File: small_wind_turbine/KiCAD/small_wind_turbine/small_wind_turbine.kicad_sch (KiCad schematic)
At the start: 50 parts, among them J1 Conn_01x03_Male, J2 Conn_01x03_Male, K1 FINDER-36.11, SW1 SW_Push_SPDT, U2 UC2844A, U3 IRS10752LPBF, U4 Opamp_Quad, U7 MCP3021, U8 MCP4725xxx-xCH, U9 AZ1117-5.0

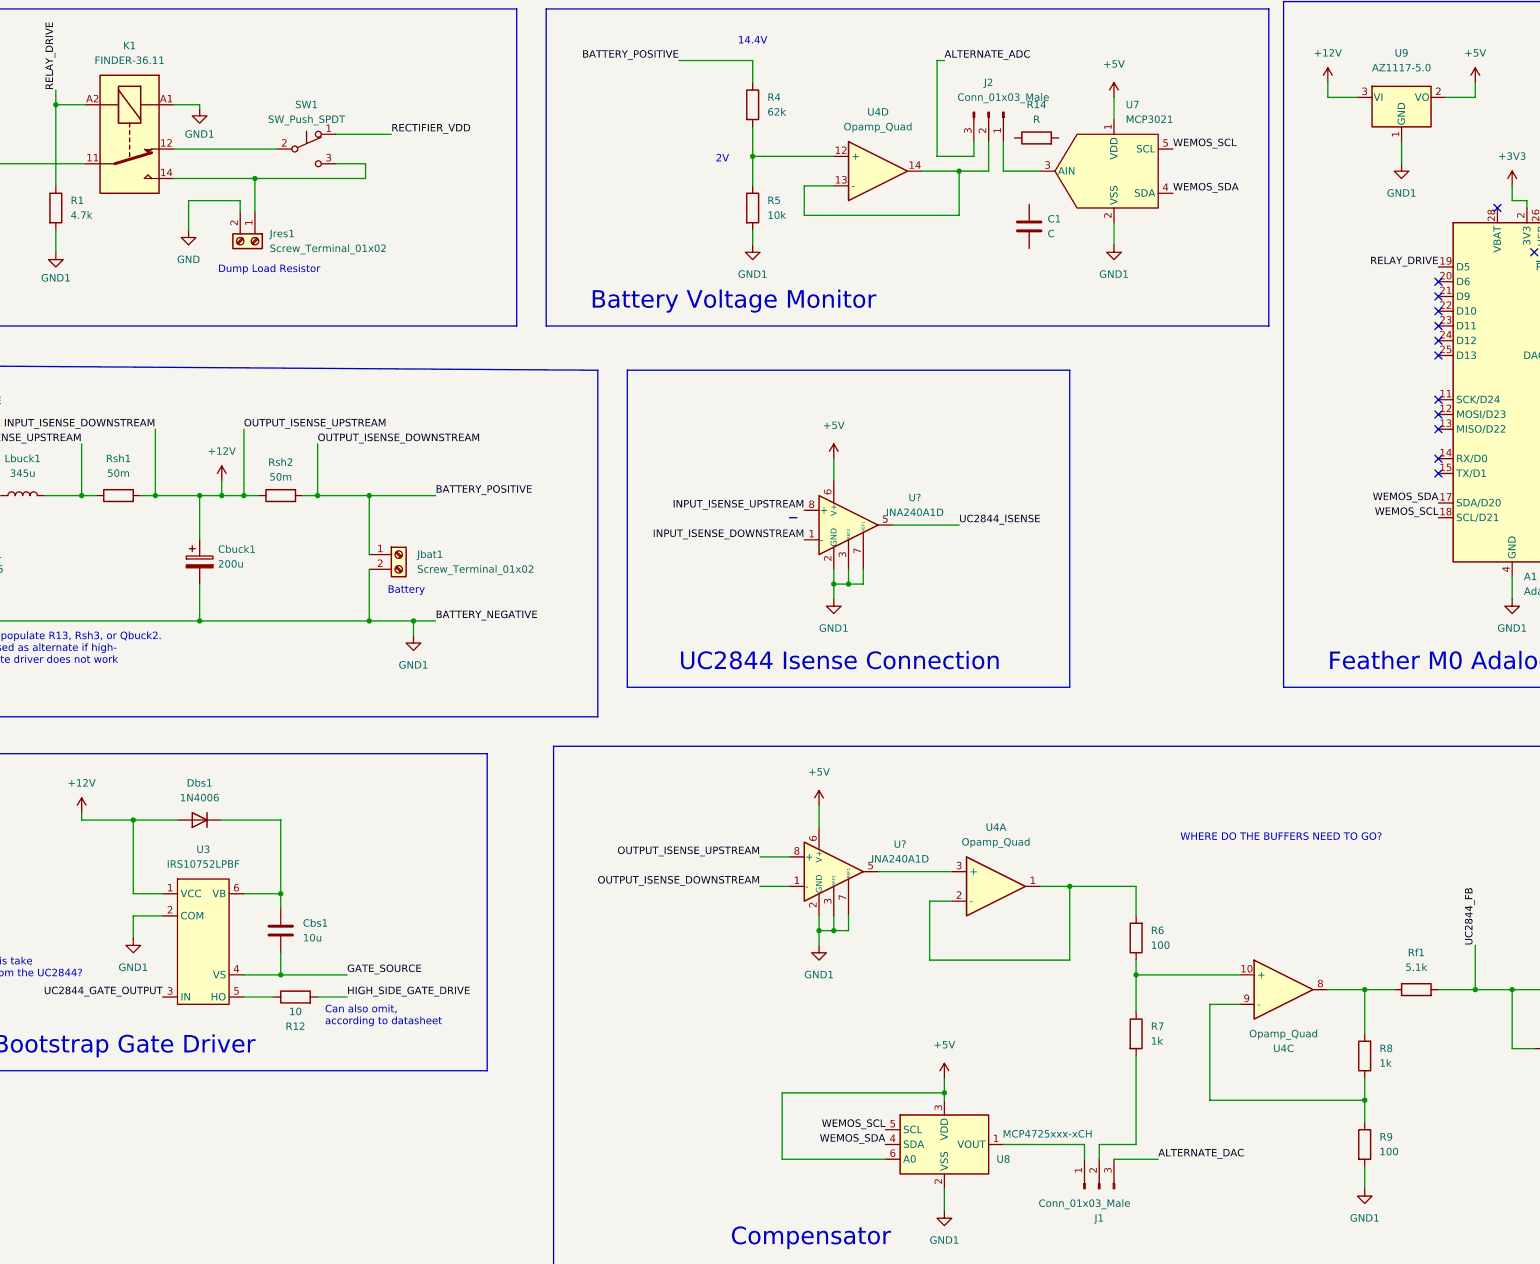
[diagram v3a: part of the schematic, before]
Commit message: update KiCAD resistor values to match PLECS model
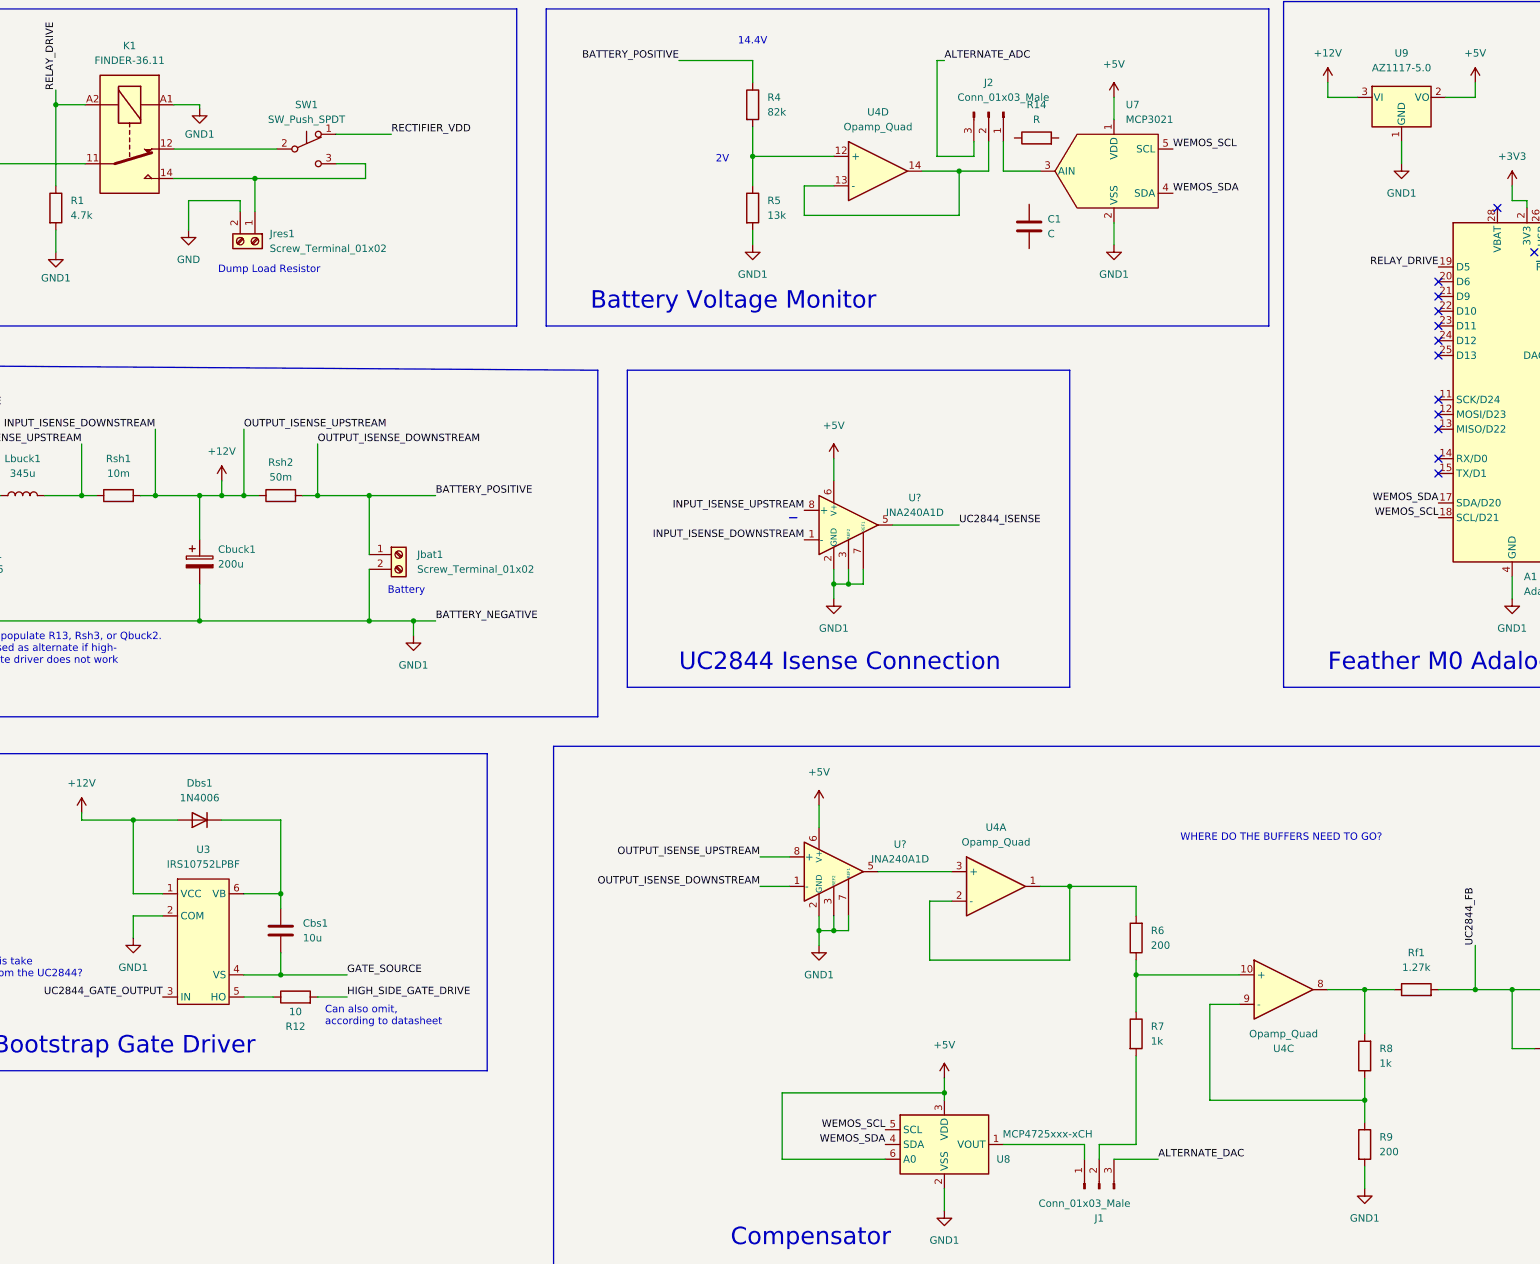
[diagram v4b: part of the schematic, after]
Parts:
- R4: value 62k -> 82k
- R5: value 10k -> 13k
- R6, R9: value 100 -> 200
- Rf1: value 5.1k -> 1.27k
- Rsh1: value 50m -> 10m
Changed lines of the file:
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@@
     (in_bom yes) (on_board yes) (fields_autoplaced)
     (property "Reference" "Rsh1" (id 0) (at 123.19 95.25 90))
-    (property "Value" "50m" (id 1) (at 123.19 97.79 90))
+    (property "Value" "10m" (id 1) (at 123.19 97.79 90))
     (property "Footprint" "" (id 2) (at 123.19 103.378 90)
       (effects (font (size 1.27 1.27)) hide)
@@
       (effects (font (size 1.27 1.27)) (justify left))
     )
-    (property "Value" "100" (id 1) (at 340.36 214.6299 0)
+    (property "Value" "200" (id 1) (at 340.36 214.6299 0)
       (effects (font (size 1.27 1.27)) (justify left))
     )
@@
       (effects (font (size 1.27 1.27)) (justify right))
     )
-    (property "Value" "100" (id 1) (at 300.99 179.0699 0)
+    (property "Value" "200" (id 1) (at 300.99 179.0699 0)
       (effects (font (size 1.27 1.27)) (justify right))
     )
@@
       (effects (font (size 1.27 1.27)) (justify left))
     )
-    (property "Value" "62k" (id 1) (at 234.95 35.5599 0)
+    (property "Value" "82k" (id 1) (at 234.95 35.5599 0)
       (effects (font (size 1.27 1.27)) (justify left))
     )
@@
       (effects (font (size 1.27 1.27)) (justify left))
     )
-    (property "Value" "10k" (id 1) (at 234.95 53.3399 0)
+    (property "Value" "13k" (id 1) (at 234.95 53.3399 0)
       (effects (font (size 1.27 1.27)) (justify left))
     )
@@
     (in_bom yes) (on_board yes) (fields_autoplaced)
     (property "Reference" "Rf1" (id 0) (at 346.71 180.34 90))
-    (property "Value" "5.1k" (id 1) (at 346.71 182.88 90))
+    (property "Value" "1.27k" (id 1) (at 346.71 182.88 90))
     (property "Footprint" "" (id 2) (at 346.71 188.468 90)
       (effects (font (size 1.27 1.27)) hide)
@@
     )
     (path "/be00c5cc-e602-4c91-a701-fb1ee4a55bb7"
-      (reference "R4") (unit 1) (value "62k") (footprint "")
+      (reference "R4") (unit 1) (value "82k") (footprint "")
     )
     (path "/c7c041c4-5b3c-4114-bd43-65ad92655c96"
-      (reference "R5") (unit 1) (value "10k") (footprint "")
+      (reference "R5") (unit 1) (value "13k") (footprint "")
     )
     (path "/4da2e1e6-5b76-4bd5-9b35-24b5f33db3c0"
-      (reference "R6") (unit 1) (value "100") (footprint "")
+      (reference "R6") (unit 1) (value "200") (footprint "")
     )
     (path "/0c39ab43-976b-404c-bc1e-3ceafeb04cbf"
@@
     )
     (path "/43aa9581-8aa4-4148-bcaa-7b4fd33948eb"
-      (reference "R9") (unit 1) (value "100") (footprint "")
+      (reference "R9") (unit 1) (value "200") (footprint "")
     )
     (path "/874347cc-2cf5-477e-b19a-e0ad8383c913"
@@
     )
     (path "/d9a98a0d-384d-4680-8a17-c665c91da68b"
-      (reference "Rf1") (unit 1) (value "5.1k") (footprint "")
+      (reference "Rf1") (unit 1) (value "1.27k") (footprint "")
     )
     (path "/37a8dcf8-039a-4420-b719-bb0b37f6045c"
-      (reference "Rsh1") (unit 1) (value "50m") (footprint "")
+      (reference "Rsh1") (unit 1) (value "10m") (footprint "")
     )
     (path "/4145bb66-9680-4e66-8c64-c9430ebfb079"

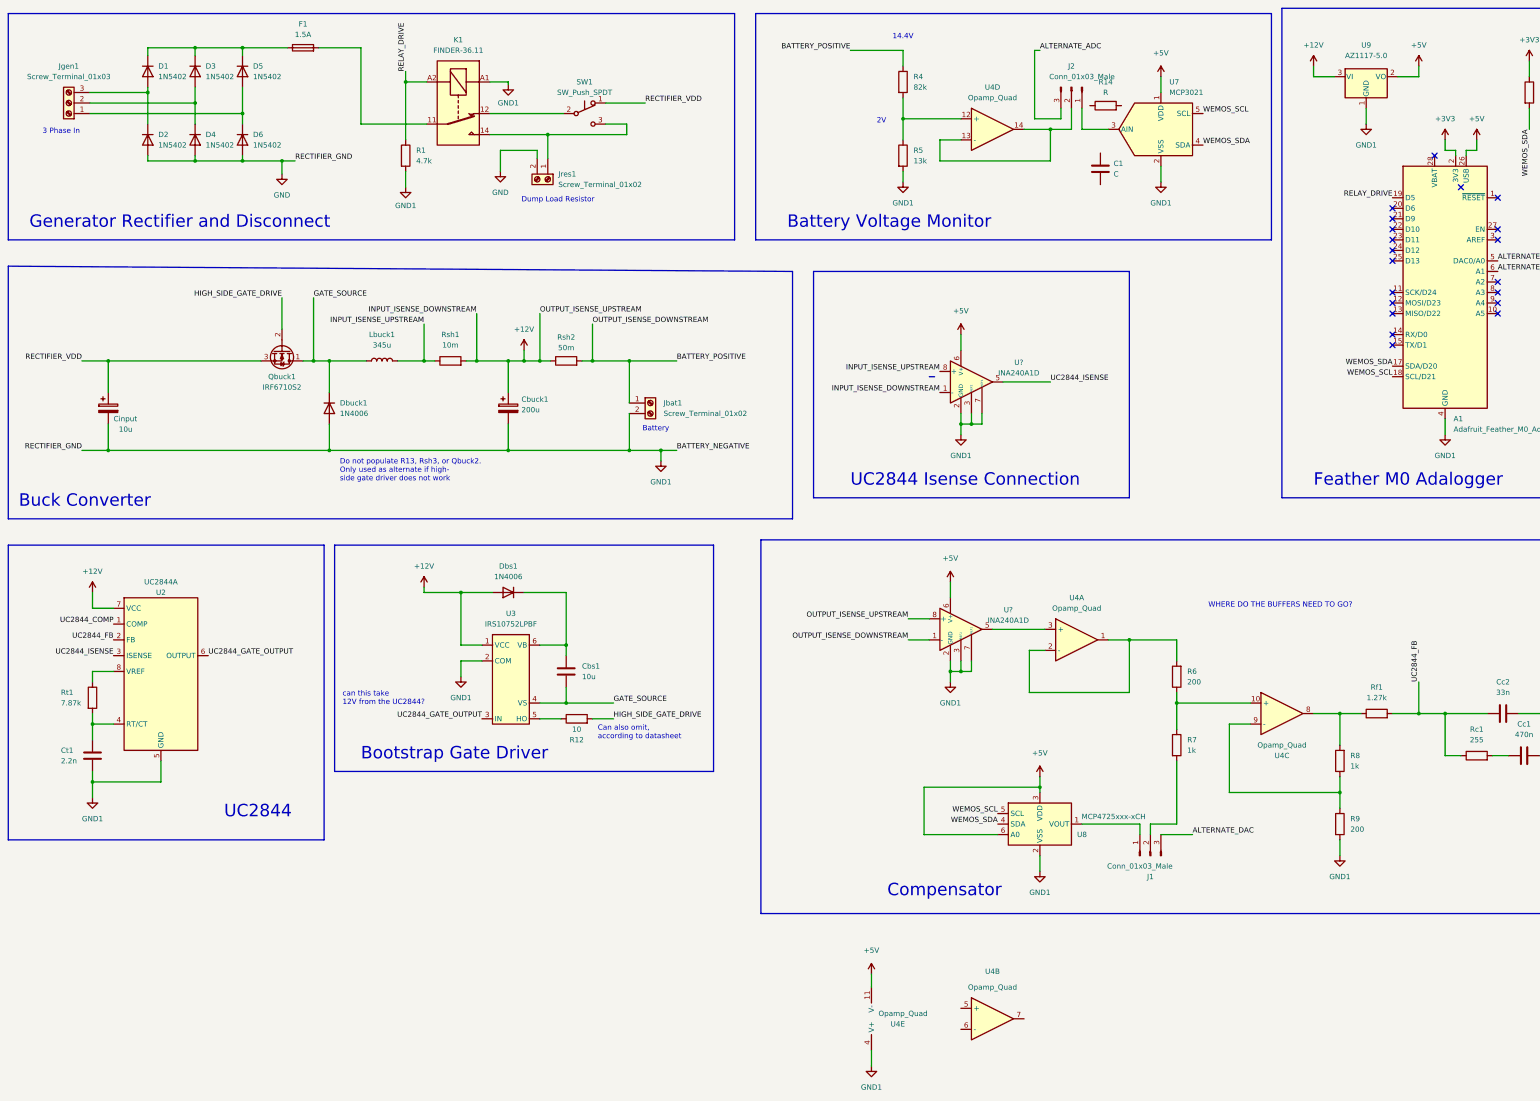
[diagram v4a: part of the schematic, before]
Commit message: start adding footprints and bypass capacitors
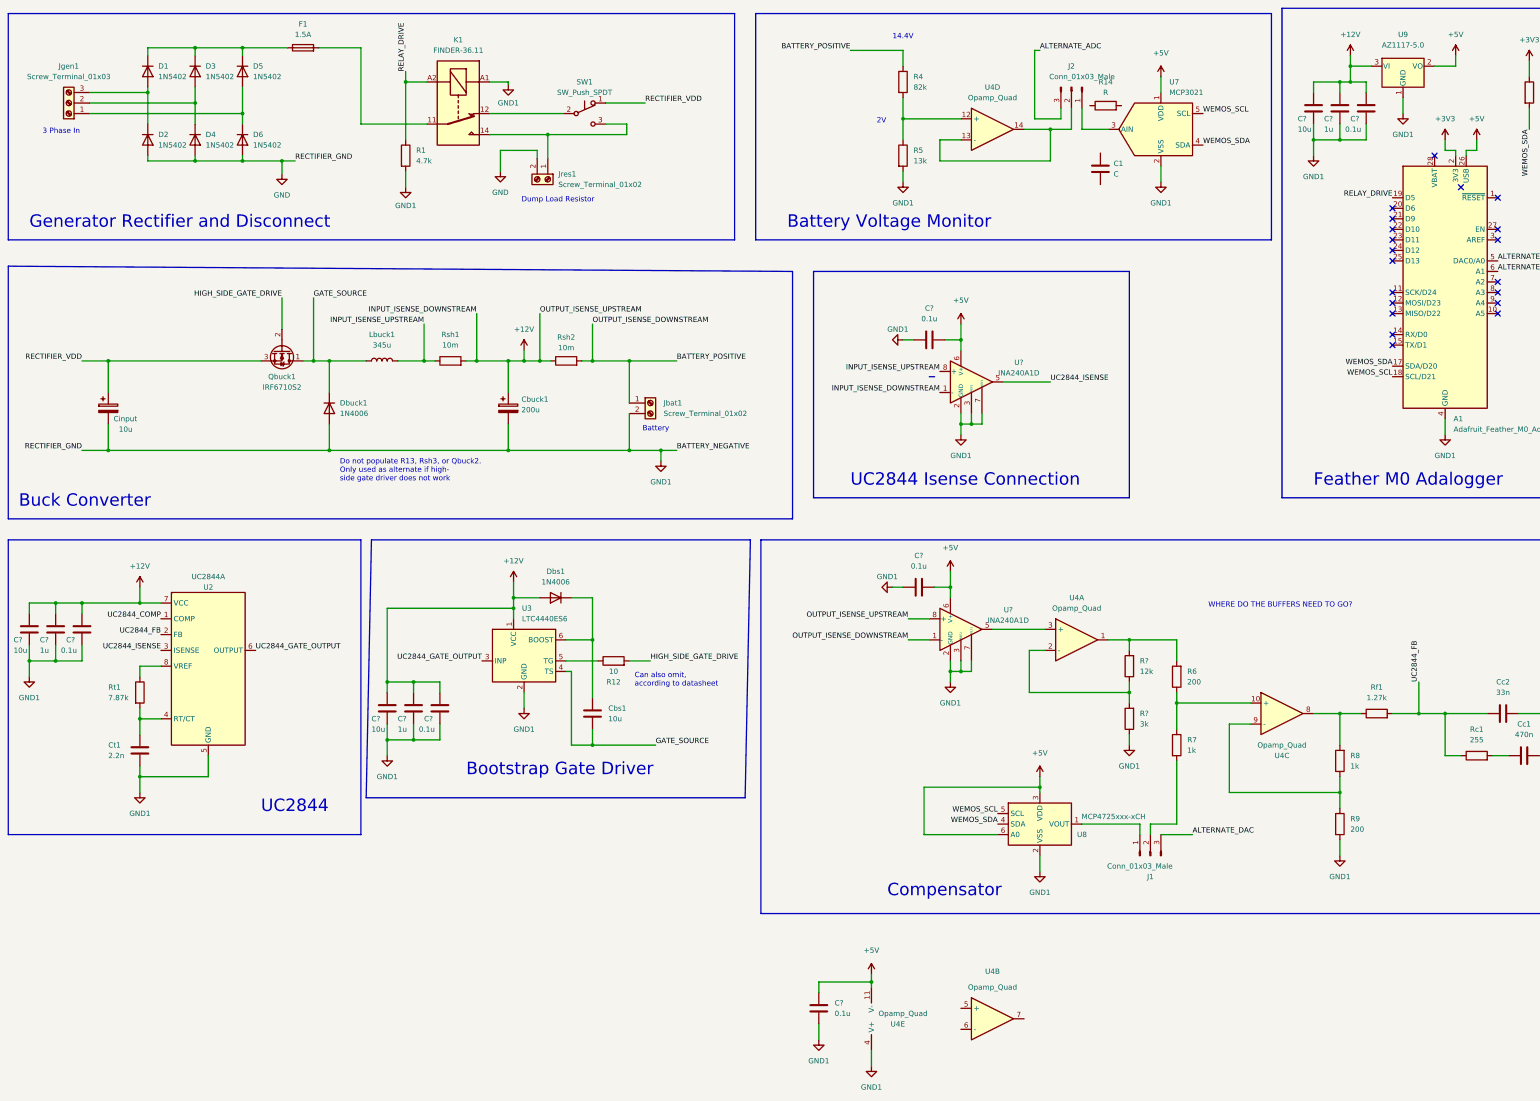
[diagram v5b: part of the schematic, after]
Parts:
- removed U3: IRS10752LPBF, symbol just_energy_hub:IRS10752LPBF
- added C? (x3): 10u, symbol Device:C
- added C? (x3): 1u, symbol Device:C
- added C? (x6): 0.1u, symbol Device:C
- added R?: 12k, symbol Device:R
- added R?: 3k, symbol Device:R
- added U3: LTC4440ES6, Package_TO_SOT_SMD:SOT-23-6, symbol Driver_FET:LTC4440ES6
- Rsh2: value 50m -> 10m
- U2: footprint (none) -> Package_SO:SOIC-8_3.9x4.9mm_P1.27mm
- U4: footprint (none) -> Package_SO:SOIC-14_3.9x8.7mm_P1.27mm
- U9: footprint (none) -> Package_TO_SOT_SMD:SOT-223-3_TabPin2
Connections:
- net +12V: now also C?.1, C?.1, C?.1, C?.1, C?.1, C?.1, C?.1, C?.1, C?.1, U3.1 (VCC)
- net +5V: now also C?.1, C?.2, C?.2
- net GATE_SOURCE: now also U3.4 (TS)
- net GND: now also C?.1, C?.1, C?.2, C?.2, C?.2, C?.2, C?.2, C?.2, C?.2, C?.2, C?.2, C?.2, R?.1, U3.2 (GND)
- net UC2844_GATE_OUTPUT: now also U3.3 (INP)
- net at R6.2, U4.1: now also R?.2; no longer U4.2 (-)
- net at R12.1: now also U3.5 (TG)
- net at Cbs1.1, Dbs1.1 (K): now also U3.6 (BOOST)
- new net: R?.1, R?.2, U4.2 (-)
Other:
- note removed: "can this take 12V from the UC2844?"
- moved on the sheet: Cbs1, Ct1, Dbs1, R12, Rt1, U2, U9

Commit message: finish assigning IC footprints and bypass capacitance. All IC footprints are double-checked.
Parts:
- added C? (x2): 10u, symbol Device:C
- added C? (x2): 0.1u, symbol Device:C
- U7: footprint (none) -> Package_TO_SOT_SMD:SOT-23-5
- gave numbers to parts that had none: 2
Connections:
- net +5V: now also U4.4 (V+), C?.1, C?.1, C?.1, C?.1; no longer U4.11 (V-)
- net GND: now also U4.11 (V-), C?.2, C?.2, C?.2, C?.2; no longer U4.4 (V+)
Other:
- moved on the sheet: C1, C?, Cbs1, Ct1, Dbs1, J2, R12, R14, R4, R5, Rt1, U2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

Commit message: wip assigning passives footprints
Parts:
- removed C1: C, symbol Device:C
- removed R14: R, symbol Device:R
- gave numbers to parts that had none: 18
- renumbered Cinput to Cinput1

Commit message: wip adding footprints (2)
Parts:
- C1, C10, C11, C12, C13, C14, C15, C16, C2, C3, C4, C5, C6, C7, C8, C9, Cbs1, Cc1, Cc2, Ct1: footprint (none) -> Capacitor_SMD:C_0805_2012Metric
- Cbuck1: footprint (none) -> Capacitor_THT:CP_Radial_D12.5mm_P5.00mm
- Cinput1: footprint (none) -> Capacitor_THT:CP_Radial_D6.3mm_P2.50mm
- D1, D2, D3, D4, D5, D6: footprint Diode_THT:D_DO-201AD_P15.24mm_Horizontal -> Package_TO_SOT_SMD:TO-277A
- Dbs1, Dbuck1: footprint Diode_THT:D_DO-41_SOD81_P10.16mm_Horizontal -> Package_TO_SOT_SMD:TO-277A
- R1, R10, R11, R12, R2, R3, R4, R5, R6, R7, R8, R9, Rc1, Rf1, Rt1: footprint (none) -> Resistor_SMD:R_0805_2012Metric
